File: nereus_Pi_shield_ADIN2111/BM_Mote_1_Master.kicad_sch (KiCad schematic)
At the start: 31 parts, among them J1 Raspberry_Pi_2_3

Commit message: S4.d: footprints findable -- project library Vault (mote.pretty) extracted from the mote board; close S5.a
43 footprints the schematic uses, extracted read-only from the reference
board with KiCad 9.0.6 pcbnew (tools/fpextract.py, back-side parts
flipped, nets cleared), registered as nickname Vault to match the board
IDs; 118 bare footprint fields -> Vault:<name>. fpextract --verify: 0
problems (negative-tested). Netlist identical except footprint fields.
ERC 74/626 -> 74/508 (footprint-link warnings gone). D19.

Co-Authored-By: Claude Opus 5.5 <noreply@anthropic.com>
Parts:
- FID1, FID2, FID3, FID4, FID5, FID6: footprint FIDUCIAL_075MM -> Vault:FIDUCIAL_075MM
- MP1, MP2, MP3, MP4: footprint 78614015360-Footprint-2 -> Vault:78614015360-Footprint-2
- MTG1, MTG2, MTG3, MTG4: footprint Hole_M3 -> Vault:Hole_M3
- R10: footprint RESC1005X40X25NL05T10 -> Vault:RESC1005X40X25NL05T10
- R11: footprint FP-CRCW1210-e3-IPC_B -> Vault:FP-CRCW1210-e3-IPC_B
- TP13, TP19, TP20, TP21, TP22, TP23, TP24, TP3, TP36, TP38, TP5, TP7, TP8: footprint PCB_TP_1.5mm -> Vault:PCB_TP_1.5mm
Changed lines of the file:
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@@
 			)
 		)
-		(property "Footprint" "Hole_M3"
+		(property "Footprint" "Vault:Hole_M3"
 			(at 328.93 321.31 0)
 			(effects
@@
 			)
 		)
-		(property "Footprint" ""
+				(property "Footprint" ""
 			(at 375.92 210.82 0)
 			(effects
@@
 			)
 		)
-		(property "Footprint" "78614015360-Footprint-2"
+		(property "Footprint" "Vault:78614015360-Footprint-2"
 			(at 485.14 121.92 0)
 			(effects
@@
 			)
 		)
-		(property "Footprint" ""
+				(property "Footprint" ""
 			(at 92.71 119.38 0)
 			(effects
@@
 			)
 		)
-		(property "Footprint" "Hole_M3"
+		(property "Footprint" "Vault:Hole_M3"
 			(at 354.33 321.31 0)
 			(effects
@@
 			)
 		)
-		(property "Footprint" "FIDUCIAL_075MM"
+		(property "Footprint" "Vault:FIDUCIAL_075MM"
 			(at 237.49 323.85 0)
 			(effects
@@
 			)
 		)
-		(property "Footprint" "FIDUCIAL_075MM"
+		(property "Footprint" "Vault:FIDUCIAL_075MM"
 			(at 267.76 324.042 0)
 			(effects
@@
 			)
 		)
-		(property "Footprint" "PCB_TP_1.5mm"
+		(property "Footprint" "Vault:PCB_TP_1.5mm"
 			(at 472.44 101.6 0)
 			(effects
@@
 			)
 		)
-		(property "Footprint" ""
+				(property "Footprint" ""
 			(at 368.3 210.82 0)
 			(effects
@@
 			)
 		)
-		(property "Footprint" "FIDUCIAL_075MM"
+		(property "Footprint" "Vault:FIDUCIAL_075MM"
 			(at 283 324.042 0)
 			(effects
@@
 			)
 		)
-		(property "Footprint" ""
+				(property "Footprint" ""
 			(at 193.04 193.04 0)
 			(effects
@@
 			)
 		)
-		(property "Footprint" "78614015360-Footprint-2"
+		(property "Footprint" "Vault:78614015360-Footprint-2"
 			(at 485.14 137.16 0)
 			(effects
@@
 			)
 		)
-		(property "Footprint" ""
+				(property "Footprint" ""
 			(at 198.12 101.6 0)
 			(effects
@@
 			)
 		)
-		(property "Footprint" "PCB_TP_1.5mm"
+		(property "Footprint" "Vault:PCB_TP_1.5mm"
 			(at 213.36 167.64 0)
 			(effects
@@
 			)
 		)
-		(property "Footprint" ""
+				(property "Footprint" ""
 			(at 361.95 106.68 0)
 			(effects
@@
 			)
 		)
-		(property "Footprint" ""
+				(property "Footprint" ""
 			(at 391.16 104.14 0)
 			(effects
@@
 			)
 		)
-		(property "Footprint" "RESC1005X40X25NL05T10"
+		(property "Footprint" "Vault:RESC1005X40X25NL05T10"
 			(at 203.2 172.72 0)
 			(effects
@@
 			)
 		)
-		(property "Footprint" "FP-CRCW1210-e3-IPC_B"
+		(property "Footprint" "Vault:FP-CRCW1210-e3-IPC_B"
 			(at 172.72 190.5 0)
 			(effects
@@
 			)
 		)
-		(property "Footprint" "Hole_M3"
+		(property "Footprint" "Vault:Hole_M3"
 			(at 341.63 321.31 0)
 			(effects
@@
 			)
 		)
-		(property "Footprint" ""
+				(property "Footprint" ""
 			(at 383.54 190.5 0)
 			(effects
@@
 			)
 		)
-		(property "Footprint" "PCB_TP_1.5mm"
+		(property "Footprint" "Vault:PCB_TP_1.5mm"
 			(at 304.8 185.42 0)
 			(effects
@@
 			)
 		)
-		(property "Footprint" "PCB_TP_1.5mm"
+		(property "Footprint" "Vault:PCB_TP_1.5mm"
 			(at 289.56 119.38 0)
 			(effects
@@
 			)
 		)
-		(property "Footprint" "PCB_TP_1.5mm"
+		(property "Footprint" "Vault:PCB_TP_1.5mm"
 			(at 375.92 208.28 0)
 			(effects
@@
 			)
 		)
-		(property "Footprint" "PCB_TP_1.5mm"
+		(property "Footprint" "Vault:PCB_TP_1.5mm"
 			(at 472.44 119.38 0)
 			(effects
@@
 			)
 		)
-		(property "Footprint" "PCB_TP_1.5mm"
+		(property "Footprint" "Vault:PCB_TP_1.5mm"
 			(at 472.44 127 0)
 			(effects
@@
 			)
 		)
-		(property "Footprint" "FIDUCIAL_075MM"
+		(property "Footprint" "Vault:FIDUCIAL_075MM"
 			(at 252.52 324.042 0)
 			(effects
@@
 			)
 		)
-		(property "Footprint" "78614015360-Footprint-2"
+		(property "Footprint" "Vault:78614015360-Footprint-2"
 			(at 485.14 106.68 0)
 			(effects
@@
 			)
 		)
-		(property "Footprint" "Hole_M3"
+		(property "Footprint" "Vault:Hole_M3"
 			(at 316.23 321.31 0)
 			(effects
@@
 			)
 		)
-		(property "Footprint" "PCB_TP_1.5mm"
+		(property "Footprint" "Vault:PCB_TP_1.5mm"
 			(at 368.3 208.28 0)
 			(effects
@@
 			)
 		)
-		(property "Footprint" "PCB_TP_1.5mm"
+		(property "Footprint" "Vault:PCB_TP_1.5mm"
 			(at 378.46 187.96 0)
 			(effects
@@
 			)
 		)
-		(property "Footprint" ""
+				(property "Footprint" ""
 			(at 299.72 187.96 0)
 			(effects
@@
 			)
 		)
-		(property "Footprint" ""
+				(property "Footprint" ""
 			(at 358.14 104.14 0)
 			(effects
@@
 			)
 		)
-		(property "Footprint" "PCB_TP_1.5mm"
+		(property "Footprint" "Vault:PCB_TP_1.5mm"
 			(at 472.44 109.22 0)
 			(effects
@@
 			)
 		)
-		(property "Footprint" "78614015360-Footprint-2"
+		(property "Footprint" "Vault:78614015360-Footprint-2"
 			(at 485.14 91.44 0)
 			(effects
@@
 			)
 		)
-		(property "Footprint" "FIDUCIAL_075MM"
+		(property "Footprint" "Vault:FIDUCIAL_075MM"
 			(at 222.25 323.85 0)
 			(effects
@@
 			)
 		)
-		(property "Footprint" "FIDUCIAL_075MM"
+		(property "Footprint" "Vault:FIDUCIAL_075MM"
 			(at 298.24 324.042 0)
 			(effects
@@
 			)
 		)
-		(property "Footprint" "PCB_TP_1.5mm"
+		(property "Footprint" "Vault:PCB_TP_1.5mm"
 			(at 124.46 203.2 0)
 			(effects
@@
 			)
 		)
-		(property "Footprint" "PCB_TP_1.5mm"
+		(property "Footprint" "Vault:PCB_TP_1.5mm"
 			(at 368.3 182.88 0)
 			(effects
@@
 			)
 		)
-		(property "Footprint" ""
+				(property "Footprint" ""
 			(at 383.54 132.08 0)
 			(effects
@@
 			)
 		)
-		(property "Footprint" ""
+				(property "Footprint" ""
 			(at 373.38 185.42 0)
 			(effects
@@
 			)
 		)
-		(property "Footprint" "Connector_PinSocket_2.54mm:PinSocket_2x20_P2.54mm_Vertical"
+				(property "Footprint" "Connector_PinSocket_2.54mm:PinSocket_2x20_P2.54mm_Vertical"
 			(at 121.92 88.9 0)
 			(effects
@@
 			)
 		)
-		(property "Footprint" ""
+				(property "Footprint" ""
 			(at 121.92 127 0)
 			(effects
@@
 			)
 		)
-		(property "Footprint" ""
+				(property "Footprint" ""
 			(at 127 127 0)
 			(effects
@@
 			)
 		)
-		(property "Footprint" ""
+				(property "Footprint" ""
 			(at 137.16 129.54 0)
 			(effects
@@
 			)
 		)
-		(property "Footprint" ""
+				(property "Footprint" ""
 			(at 137.16 134.62 0)
 			(effects
@@
 			)
 		)
-		(property "Footprint" "PCB_TP_1.5mm"
+		(property "Footprint" "Vault:PCB_TP_1.5mm"
 			(at 368.3 195.58 0)
 			(effects
@@
 			)
 		)
-		(property "Footprint" "nereus:SolderJumper-2_R1210_Bridged_NetTie"
+				(property "Footprint" "nereus:SolderJumper-2_R1210_Bridged_NetTie"
 			(at 120.65 40.64 0)
 			(effects
@@
 			)
 		)
-		(property "Footprint" ""
+				(property "Footprint" ""
 			(at 106.68 45.72 0)
 			(effects

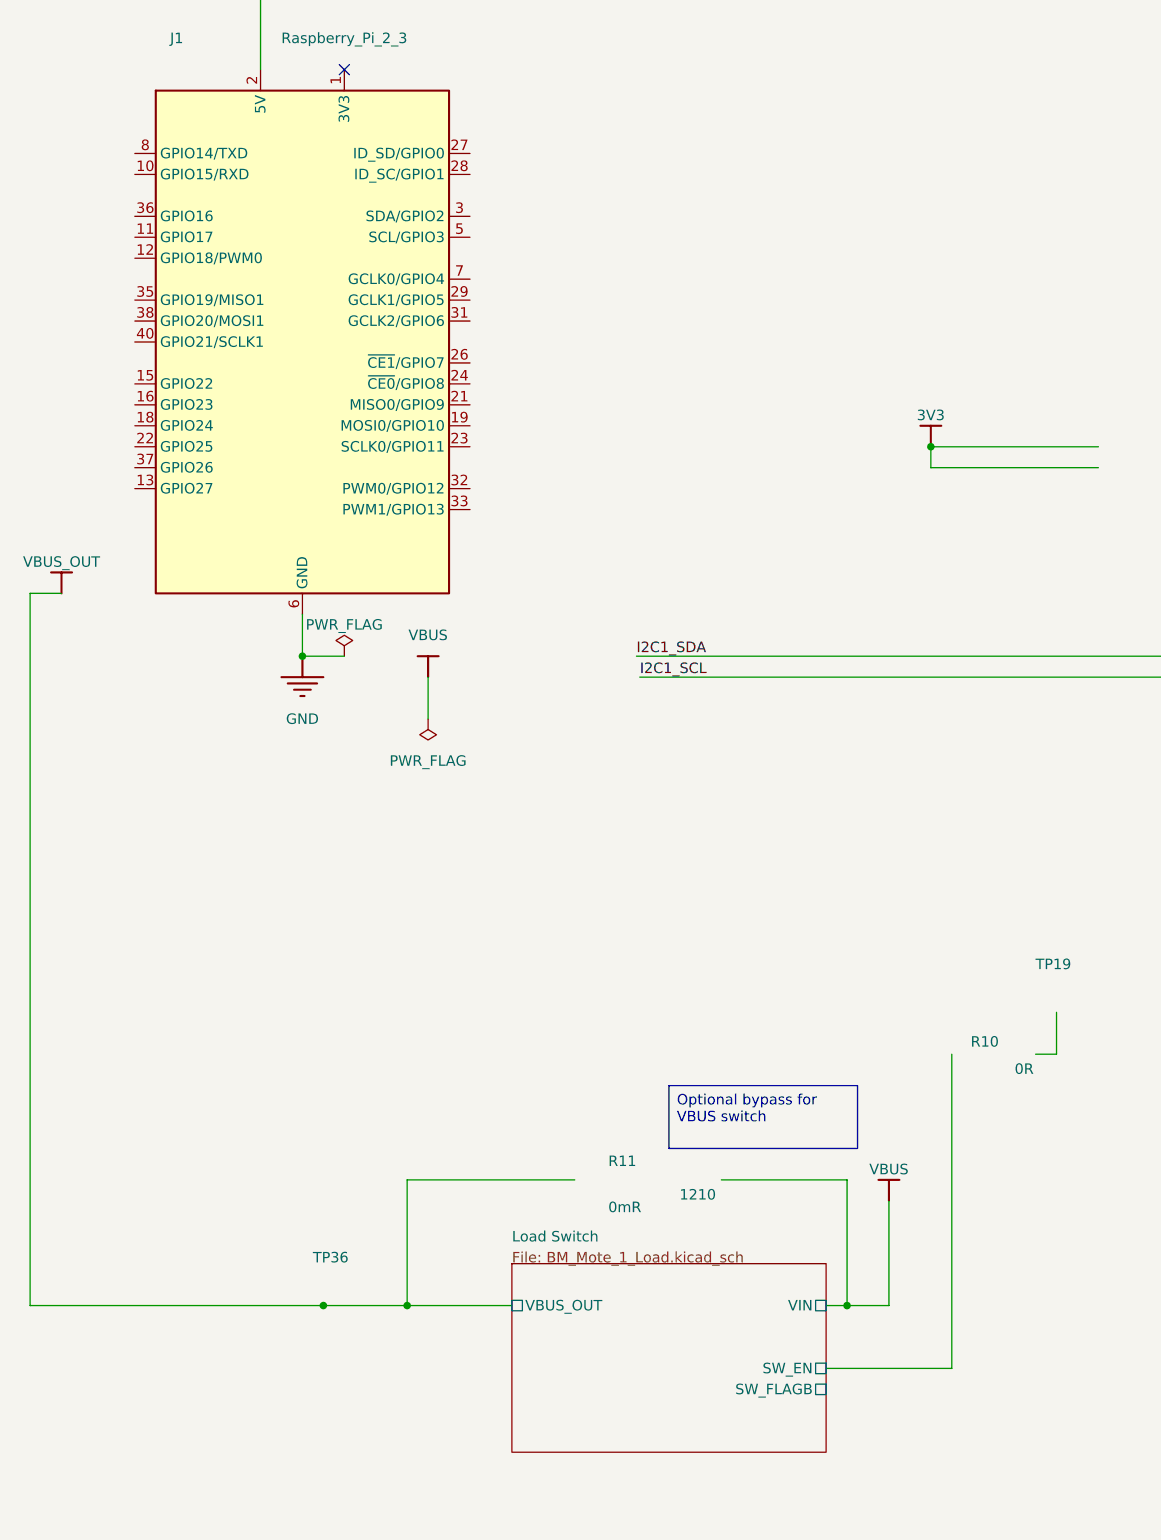
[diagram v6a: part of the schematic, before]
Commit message: S5.b: wire the Pi header -- 11 signal pins stubbed + labelled, 17 unused GPIO no-connect; close S4
J1 pins 3/5 I2C1_SDA/SCL; 19/21/23/24 ADIN_MOSI/MISO/SCK/NSS; 22 ADIN_INT;
18 ADIN_RST; 16 ADIN_PWR; 36 SW_EN; 38 SW_FLAGB. SW_EN label on the R10.1 /
sheet-pin wire; SW_FLAGB sheet pin stubbed. ERC 74/508 -> 27/508 (-29
pin_not_connected, -18 label_dangling); netcheck 50/50; midwire 0; netlist diff
= one J1 pin per net. schedit.add_label right-justifies 180-degree labels.

Co-Authored-By: Claude Opus 5.5 <noreply@anthropic.com>
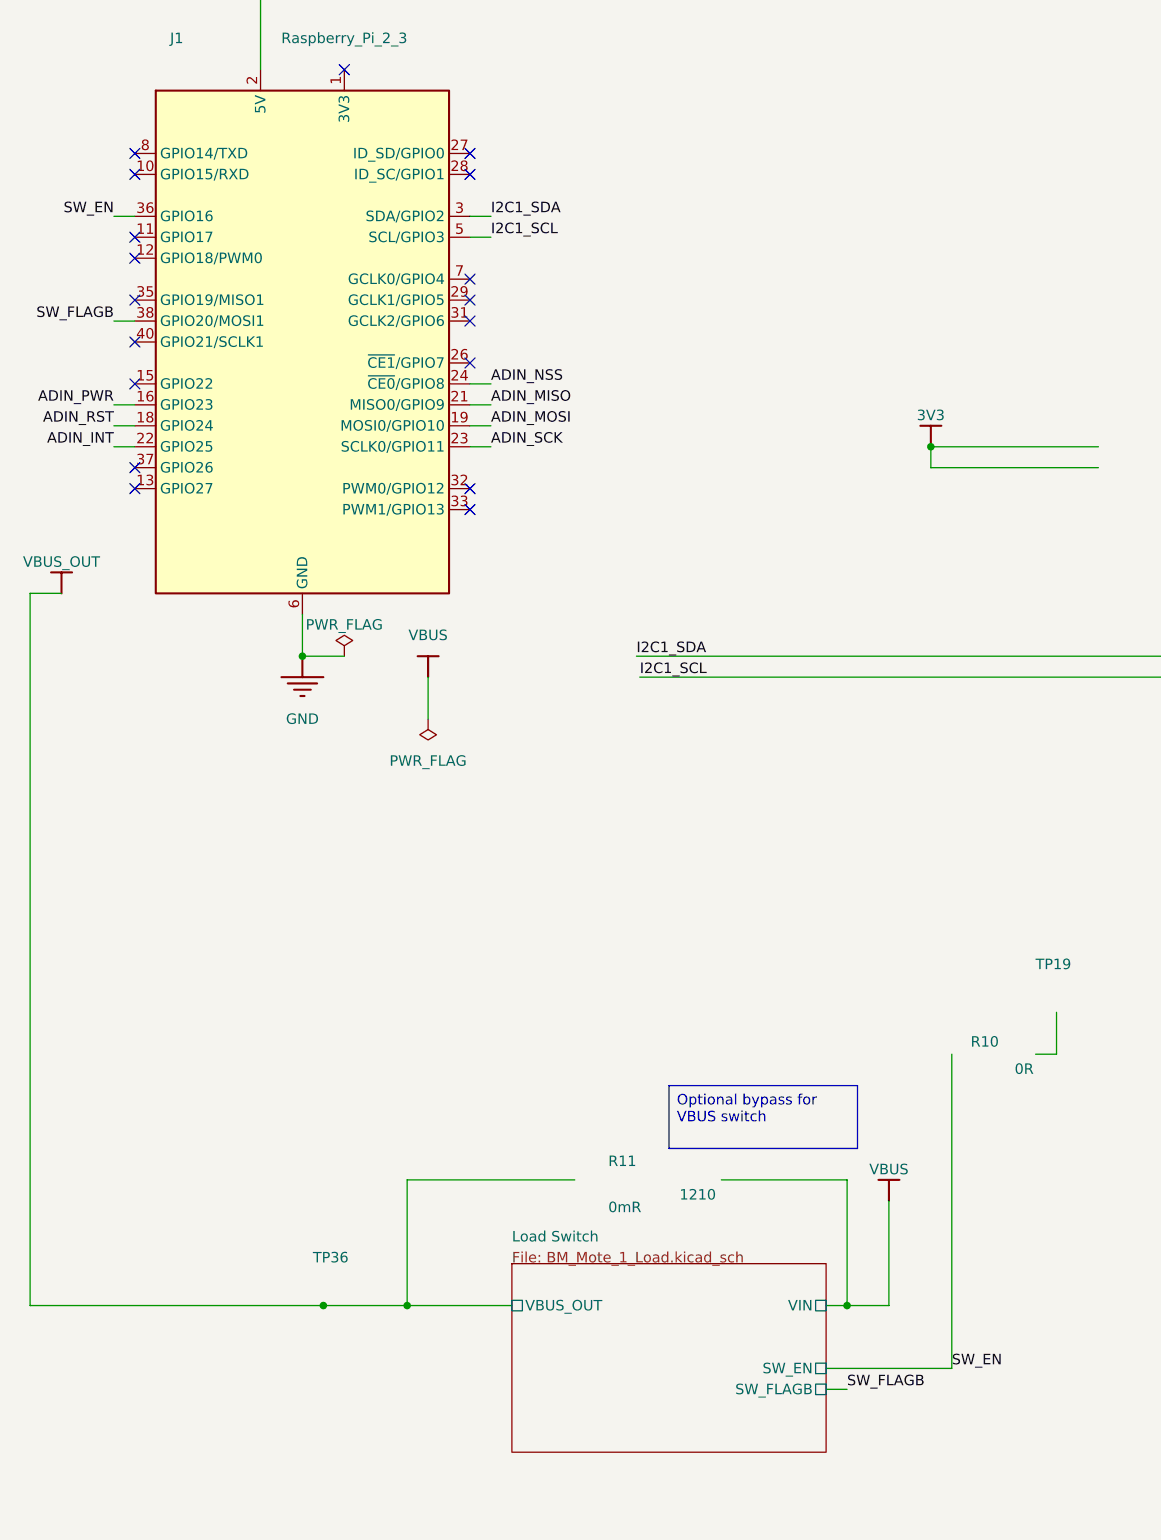
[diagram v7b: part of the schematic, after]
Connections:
- net ADIN_INT: now also J1.22 (GPIO25)
- net ADIN_MISO: now also J1.21 (MISO0/GPIO9)
- net ADIN_MOSI: now also J1.19 (MOSI0/GPIO10)
- net ADIN_NSS: now also J1.24 (~{CE0}/GPIO8)
- net ADIN_PWR: now also J1.16 (GPIO23)
- net ADIN_RST: now also J1.18 (GPIO24)
- net ADIN_SCK: now also J1.23 (SCLK0/GPIO11)
- net I2C1_SCL: now also J1.5 (SCL/GPIO3)
- net I2C1_SDA: now also J1.3 (SDA/GPIO2)
- net SW_EN: now reaches J1.36 (GPIO16)
- net SW_FLAGB: now reaches J1.38 (GPIO20/MOSI1)
- no-connect marks 1 -> 18

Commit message: S5.c: I2C pull-ups R26/R27, ADIN_PWR pull-down R43, R10 removed; ADIN power-up order documented
R26/R27 = Sofar's 4.7k ERJ-2RKF4701X to shield 3V3 (same refs/footprint, netcheck
50/50 -> 51/51). R43 100k (R21's part) keeps the ADIN off unless the Pi drives
GPIO23 (AP22913 ON has no pull-down). R10 removed, TP19 tied to SW_EN (Pi is the
only controller). DESIGN D20-D22 + 'ADIN power and boot' (strap table, boot
order, back-power cases; Option 1 software). ERC 27/508 unchanged. New
schedit.clone_symbol + test.

Co-Authored-By: Claude Opus 5.5 <noreply@anthropic.com>
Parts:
- removed R10: RC0402JR-070RL, Vault:RESC1005X40X25NL05T10, symbol BM_Mote_000639-AB-altium-import:Designator_0_RES_Altium Content Vault_0
- added R26, R27: ERJ-2RKF4701X, Vault:RESC1005X40X25LL05T05, symbol BM_Mote_000639-AB-altium-import:ADIN_0_RES-2_Altium Content Vault
- added R43: RMCF0402FT100K, Vault:FP-RMCF0402-IPC_C, symbol BM_Mote_000639-AB-altium-import:POWER_3_1029c3af85768c4190bb7ad29bc67b5_Altium 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
